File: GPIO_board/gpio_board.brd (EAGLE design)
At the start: 100 x 80 mm, 15 parts, among them J1 SWITCHES, J2 LED1, J3 LED2, Q1 IRF520, Q2 IRF520, Q3 IRF520, X1 PCI-E-164SLOT

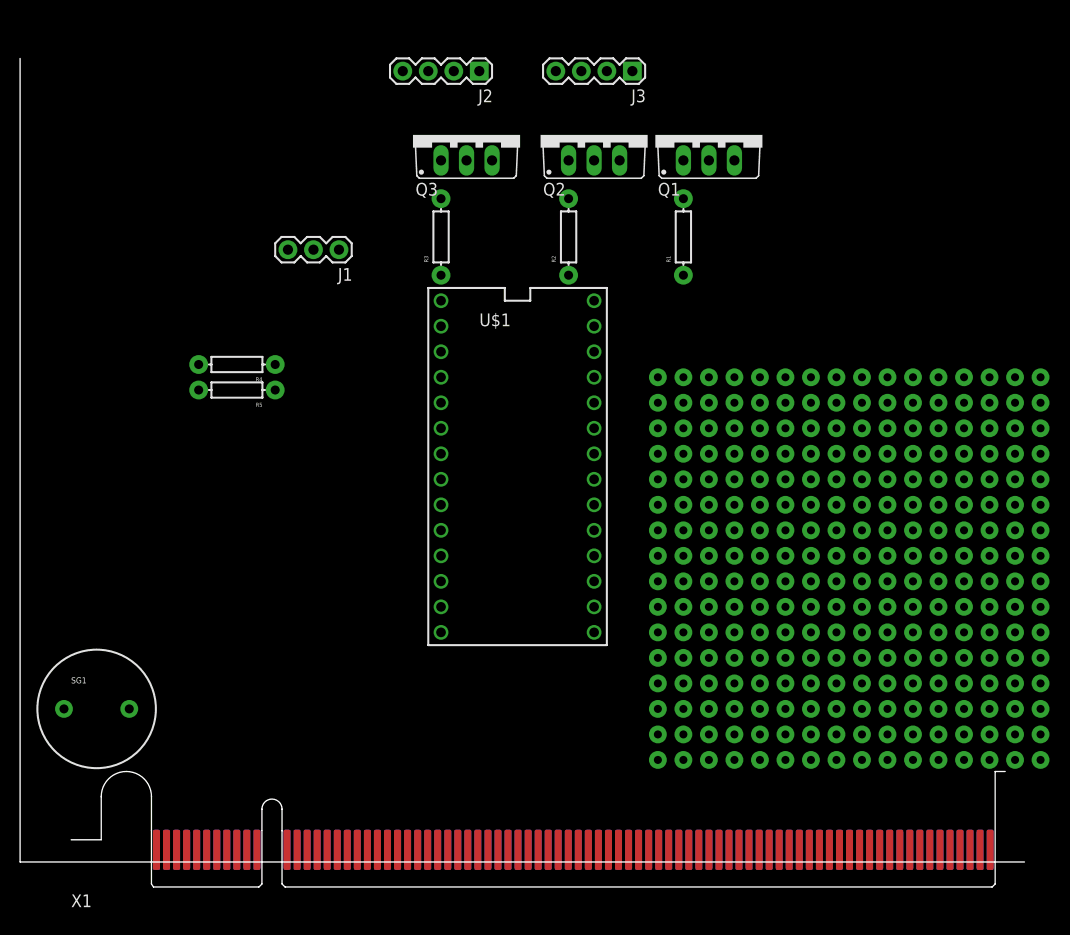
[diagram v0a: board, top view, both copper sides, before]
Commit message: routed some things
not final. need to finish outline and dimensions of board. need to
determine what other things need to go through the PCI connector (If
any).
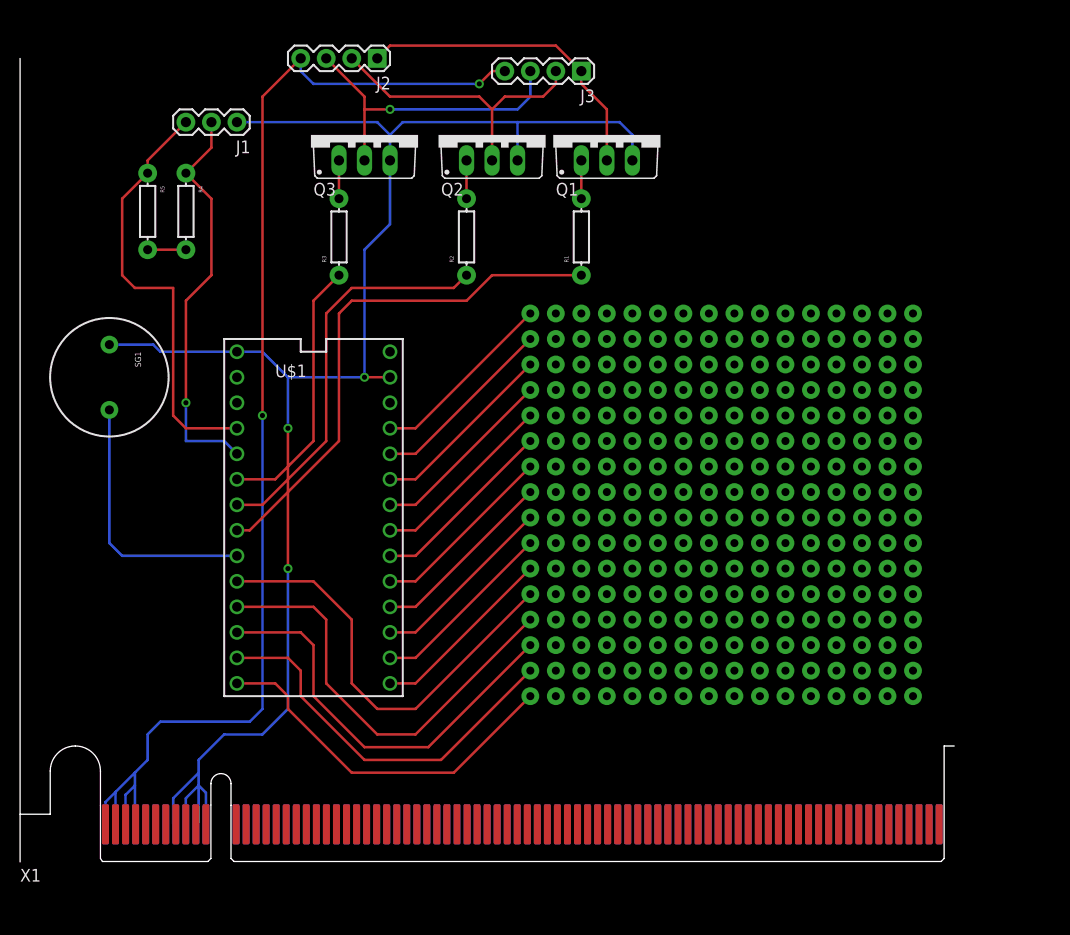
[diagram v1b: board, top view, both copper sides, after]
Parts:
- moved SG1 33.0 mm to (8.89, 48.3), turned to 270 degrees
- moved U$1 20.9 mm to (29.2, 34.3)
- moved R5 19.9 mm to (12.7, 64.8), turned to 270 degrees
- moved J1 16.3 mm to (21.6, 73.7)
- moved R4 16.1 mm to (16.5, 64.8), turned to 270 degrees
- moved U$2 14.2 mm to (50.8, 54.6)
- moved J2 10.2 mm to (35.6, 80.0)
- moved Q3 10.2 mm to (34.3, 72.4)
- moved R1 10.2 mm to (55.9, 62.2)
- moved Q1 10.2 mm to (58.4, 72.4)
- moved Q2 10.2 mm to (47.0, 72.4)
- moved R2 10.2 mm to (44.5, 62.2)
- moved R3 10.2 mm to (31.8, 62.2)
- moved X1 5.68 mm to (0.00, 0.00)
- moved J3 5.08 mm to (55.9, 78.7)
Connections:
- net GND: now also X1.A10, X1.A11, X1.A8, X1.A9
- net N$11: now also U$1.6; no longer U$1.4
- net N$8: now also U$1.4; no longer U$1.6
- net VCC: now also J2.4, J3.4, X1.A1, X1.A2, X1.A3, X1.A4
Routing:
- net GND: track 0.00 -> 167.3 mm, vias 0 -> 3
- net VCC: track 0.00 -> 124.9 mm, vias 0 -> 2
- net N$11: track 0.00 -> 52.3 mm
- net N$5: track 0.00 -> 43.1 mm
- net N$25: track 0.00 -> 42.9 mm
- net N$13: track 0.00 -> 42.9 mm
- net N$26: track 0.00 -> 41.1 mm
- net N$7: track 0.00 -> 40.5 mm, vias 0 -> 1
- net N$9: track 0.00 -> 39.8 mm
- net N$27: track 0.00 -> 38.6 mm
- net N$28: track 0.00 -> 36.8 mm
- net N$4: track 0.00 -> 31.8 mm
- net N$10: track 0.00 -> 31.3 mm, vias 0 -> 1
- net N$6: track 0.00 -> 29.8 mm
- net N$8: track 0.00 -> 26.8 mm
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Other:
- board size 100 x 80 mm -> 93 x 11.5 mm

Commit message: added sides. need to figure out discontinuity with PCIe connector
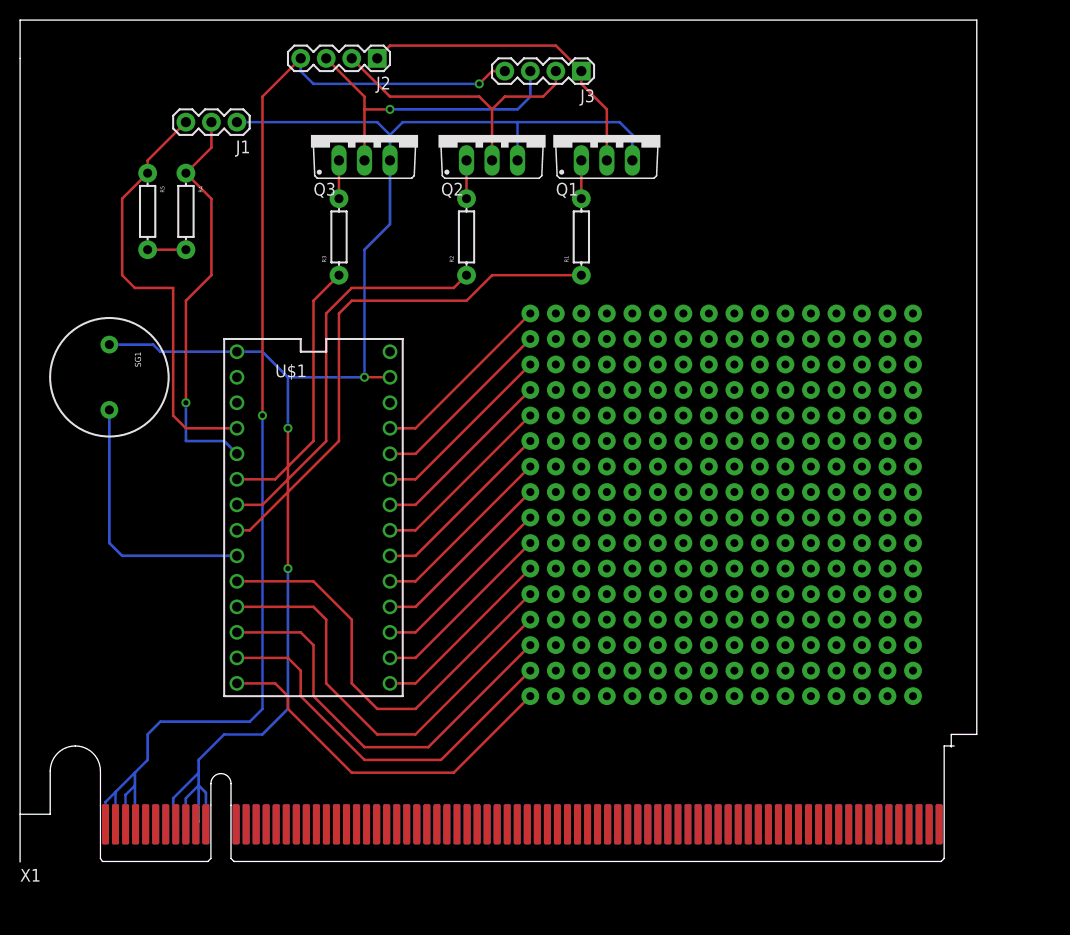
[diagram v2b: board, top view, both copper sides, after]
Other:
- board size 93 x 11.5 mm -> 95.2 x 83.8 mm
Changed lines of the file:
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@@
 <wire x1="0" y1="0" x2="0" y2="80" width="0" layer="20"/>
 <dimension x1="0" y1="0" x2="0" y2="80" x3="-27.94" y3="40" textsize="1.778" layer="20"/>
+<wire x1="0" y1="80.01" x2="0" y2="83.82" width="0" layer="20"/>
+<wire x1="0" y1="83.82" x2="95.25" y2="83.82" width="0" layer="20"/>
+<wire x1="95.25" y1="83.82" x2="95.25" y2="12.7" width="0" layer="20"/>
+<wire x1="95.25" y1="12.7" x2="92.71" y2="12.7" width="0" layer="20"/>
+<wire x1="92.71" y1="12.7" x2="92.71" y2="11.43" width="0" layer="20"/>
+<dimension x1="0" y1="83.82" x2="95.25" y2="83.82" x3="47.625" y3="91.44" textsize="1.778" layer="20"/>
 </plain>
 <attributes>

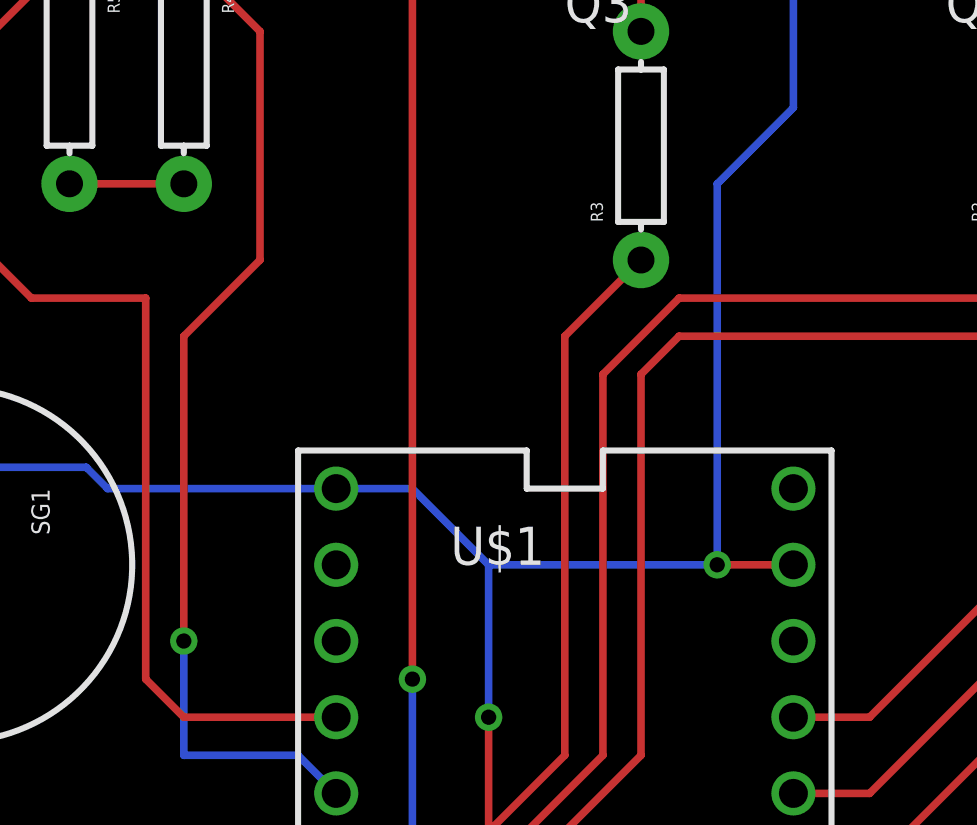
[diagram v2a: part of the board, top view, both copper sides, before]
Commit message: routed all connections
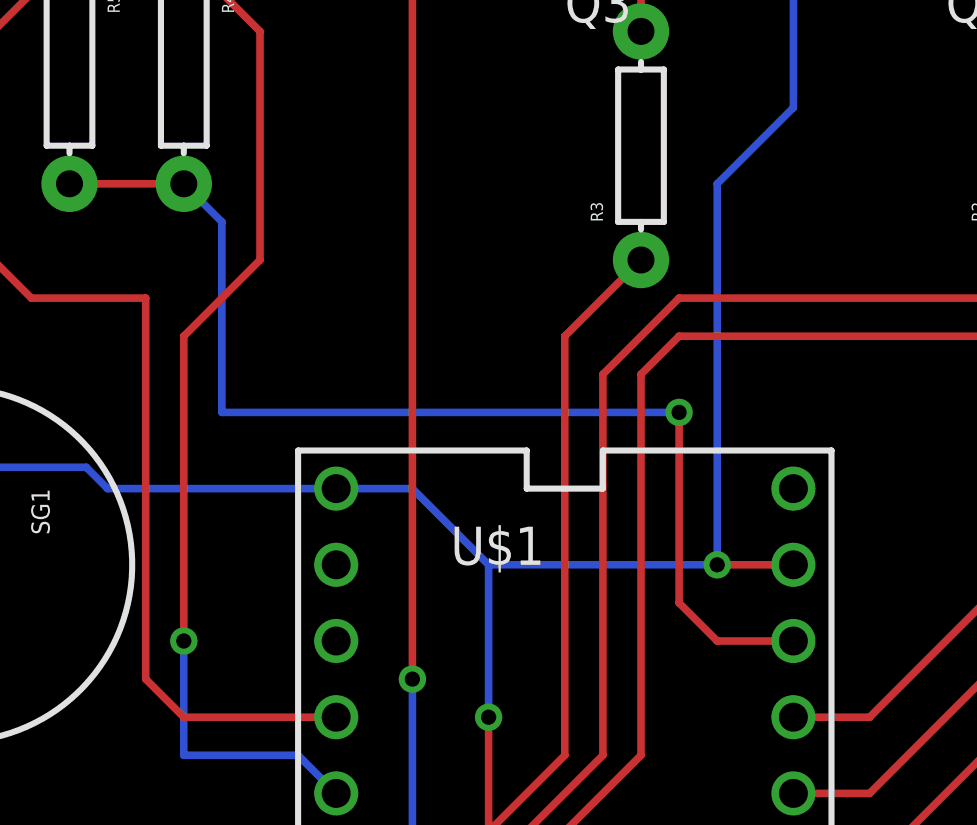
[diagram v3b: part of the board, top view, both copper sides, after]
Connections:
- net 3.3V: now also U$1.3.3V
- net VCC: no longer U$1.3.3V
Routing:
- net 3.3V: track 3.81 -> 37.9 mm, vias 0 -> 1
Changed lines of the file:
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@@
 </signal>
 <signal name="VCC">
-<contactref element="U$1" pad="3.3V"/>
 <contactref element="X1" pad="A1"/>
 <contactref element="X1" pad="A2"/>
@@
 <wire x1="11.43" y1="7.62" x2="11.43" y2="3.82" width="0.254" layer="16"/>
 <wire x1="11.43" y1="3.82" x2="11.5" y2="3.75" width="0.254" layer="16"/>
-<wire x1="36.83" y1="45.72" x2="24.13" y2="44.45" width="0" layer="19" extent="1-1"/>
 <wire x1="48.26" y1="78.74" x2="46.99" y2="78.74" width="0.254" layer="1"/>
 <wire x1="46.99" y1="78.74" x2="45.72" y2="77.47" width="0.254" layer="1"/>
@@
 <contactref element="R5" pad="P$2"/>
 <wire x1="12.7" y1="60.96" x2="16.51" y2="60.96" width="0.254" layer="1"/>
+<contactref element="U$1" pad="3.3V"/>
+<wire x1="36.83" y1="45.72" x2="34.29" y2="45.72" width="0.254" layer="1"/>
+<wire x1="34.29" y1="45.72" x2="33.02" y2="46.99" width="0.254" layer="1"/>
+<wire x1="33.02" y1="46.99" x2="33.02" y2="53.34" width="0.254" layer="1"/>
+<via x="33.02" y="53.34" extent="1-16" drill="0.508"/>
+<wire x1="33.02" y1="53.34" x2="17.78" y2="53.34" width="0.254" layer="16"/>
+<wire x1="17.78" y1="53.34" x2="17.78" y2="59.69" width="0.254" layer="16"/>
+<wire x1="17.78" y1="59.69" x2="16.51" y2="60.96" width="0.254" layer="16"/>
 </signal>
 <signal name="N$5">
